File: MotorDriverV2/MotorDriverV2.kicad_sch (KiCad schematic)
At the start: 36 parts, among them IC1 DRV8871, IC2 DRV8871, IC3 ESP32-S3-WROOM-1U-N4, J1 Power, J2 Out_A, J3 Conn_01x02_Pin, J4 Conn_01x05_Pin, J5 Conn_01x05_Pin, J6 Out_B, J7 Conn_01x02_Pin, J8 USB_C, U1 USBLC6-2SC6

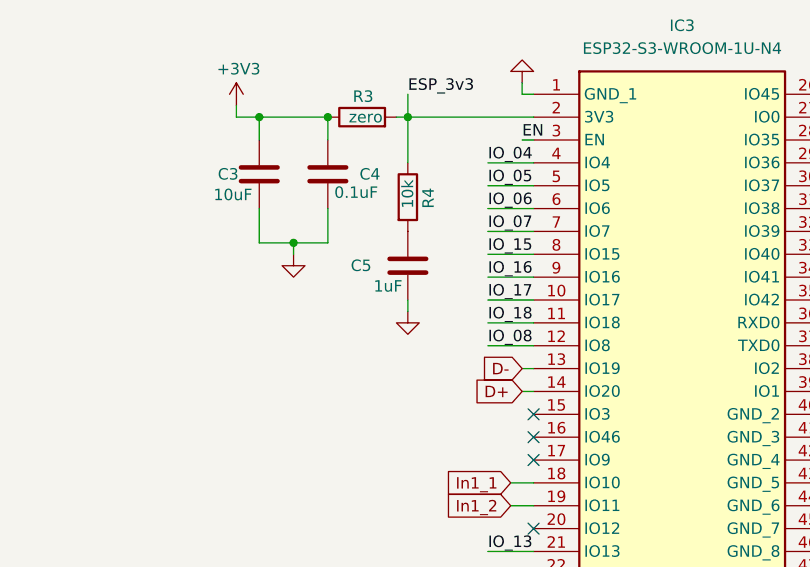
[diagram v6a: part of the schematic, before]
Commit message: UPDATE: Fix EN pin in ESP motor driver
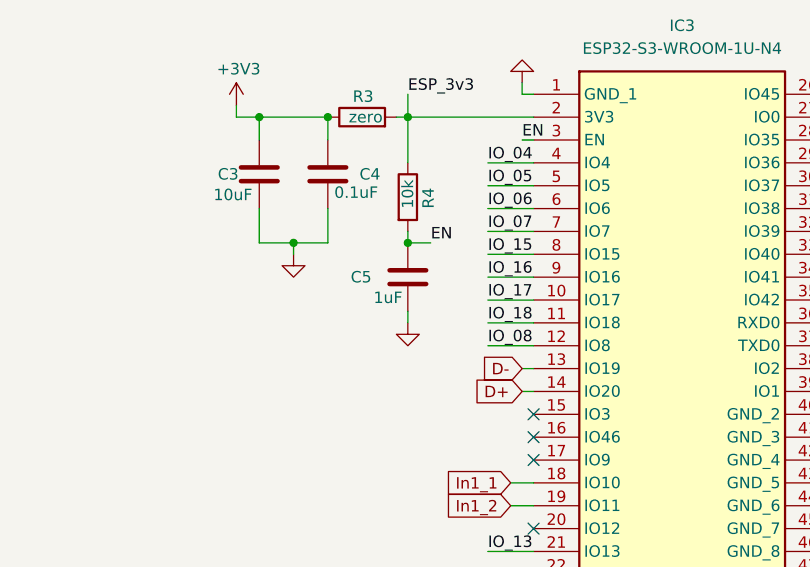
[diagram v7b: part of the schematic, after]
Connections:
- net EN: now also C5.1, R4.2
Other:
- moved on the sheet: C5
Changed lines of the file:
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@@
 	)
 	(junction
+		(at 110.49 59.69)
+		(diameter 0)
+		(color 0 0 0 0)
+	)
+	(junction
 		(at 50.8 177.8)
 		(diameter 0)
@@
 	(wire
 		(pts
+			(xy 110.49 59.69) (xy 110.49 58.42)
+		)
+		(stroke
+			(width 0)
+			(type default)
+		)
+	)
+	(wire
+		(pts
 			(xy 209.55 26.67) (xy 212.09 26.67)
 		)
@@
 	(wire
 		(pts
-			(xy 110.49 66.04) (xy 110.49 67.31)
+			(xy 110.49 67.31) (xy 110.49 68.58)
 		)
 		(stroke
@@
 	(wire
 		(pts
+			(xy 110.49 59.69) (xy 113.03 59.69)
+		)
+		(stroke
+			(width 0)
+			(type default)
+		)
+	)
+	(wire
+		(pts
 			(xy 157.48 45.72) (xy 158.75 45.72)
 		)
@@
 		)
 	)
+	(label "EN"
+		(at 113.03 59.69 0)
+		(effects
+			(font
+				(size 1.27 1.27)
+			)
+			(justify left bottom)
+		)
+	)
 	(label "IO_04"
 		(at 31.75 87.63 0)
@@
 	(symbol
 		(lib_id "Device:C")
-		(at 110.49 62.23 0)
+		(at 110.49 63.5 0)
 		(unit 1)
 		(body_style 1)
@@
 		(dnp no)
 		(property "Reference" "C5"
-			(at 104.14 62.23 0)
+			(at 104.14 63.5 0)
 			(show_name no)
 			(do_not_autoplace no)
@@
 		)
 		(property "Value" "1uF"
-			(at 106.68 64.516 0)
+			(at 106.68 65.786 0)
 			(show_name no)
 			(do_not_autoplace no)
@@
 		)
 		(property "Footprint" "Capacitor_SMD:C_0805_2012Metric_Pad1.18x1.45mm_HandSolder"
-			(at 111.4552 66.04 0)
+			(at 111.4552 67.31 0)
 			(hide yes)
 			(show_name no)
@@
 		)
 		(property "Datasheet" ""
-			(at 110.49 62.23 0)
+			(at 110.49 63.5 0)
 			(hide yes)
 			(show_name no)
@@
 		)
 		(property "Description" "Unpolarized capacitor"
-			(at 110.49 62.23 0)
+			(at 110.49 63.5 0)
 			(hide yes)
 			(show_name no)
@@
 	(symbol
 		(lib_id "power:GND")
-		(at 110.49 67.31 0)
+		(at 110.49 68.58 0)
 		(unit 1)
 		(body_style 1)
@@
 		(dnp no)
 		(property "Reference" "#PWR015"
-			(at 110.49 73.66 0)
+			(at 110.49 74.93 0)
 			(hide yes)
 			(show_name no)
@@
 		)
 		(property "Value" "GND"
-			(at 110.49 72.39 0)
+			(at 110.49 73.66 0)
 			(hide yes)
 			(show_name no)
@@
 		)
 		(property "Footprint" ""
-			(at 110.49 67.31 0)
+			(at 110.49 68.58 0)
 			(hide yes)
 			(show_name no)
@@
 		)
 		(property "Datasheet" ""
-			(at 110.49 67.31 0)
+			(at 110.49 68.58 0)
 			(hide yes)
 			(show_name no)
@@
 		)
 		(property "Description" "Power symbol creates a global label with name \"GND\" , ground"
-			(at 110.49 67.31 0)
+			(at 110.49 68.58 0)
 			(hide yes)
 			(show_name no)
